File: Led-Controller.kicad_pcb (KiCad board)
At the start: 2 copper layers, 74.3 x 47.4 mm, 103 parts, among them J1 Program, J2 Barrel_Jack, J3 Screw_Terminal, J4 Screw_Terminal, J5 Ws2812 Conn, J6 Screw_Terminal, Q1 CSD18540Q5B, Q2 CSD18540Q5B, Q3 CSD18540Q5B, Q4 CSD18540Q5B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

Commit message: Review done
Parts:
- added C39: 33u, Capacitor_SMD:C_0603_1608Metric, F.Cu at (155.3, 102.3)
- added C40: 33u, Capacitor_SMD:C_0603_1608Metric, F.Cu at (157.0, 102.3)
- added H1: MountingHole, MountingHole:MountingHole_3.2mm_M3_DIN965_Pad, F.Cu at (171.8, 103.6)
- added H2: MountingHole, MountingHole:MountingHole_3.2mm_M3_DIN965_Pad, F.Cu at (107.3, 103.8)
- moved TP2 3.75 mm to (156.5, 105.6)
- moved J3 0.13 mm to (132.1, 64.1)
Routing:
- net +3.3V: track 55.4 -> 48.1 mm
- net GND: vias 117 -> 124
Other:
- board size 74.3 x 47.4 mm -> 72.1 x 47.4 mm

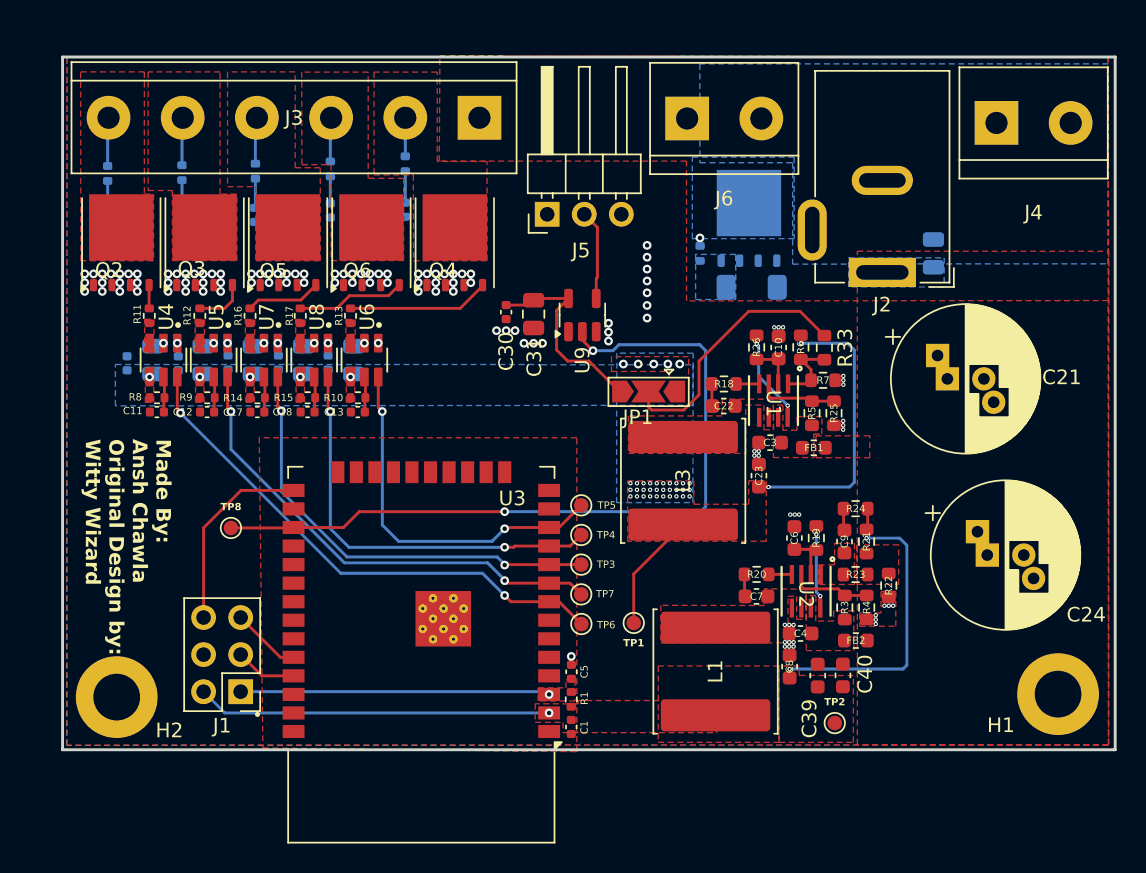
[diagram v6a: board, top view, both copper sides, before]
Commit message: WIP::Added: BOM for major components
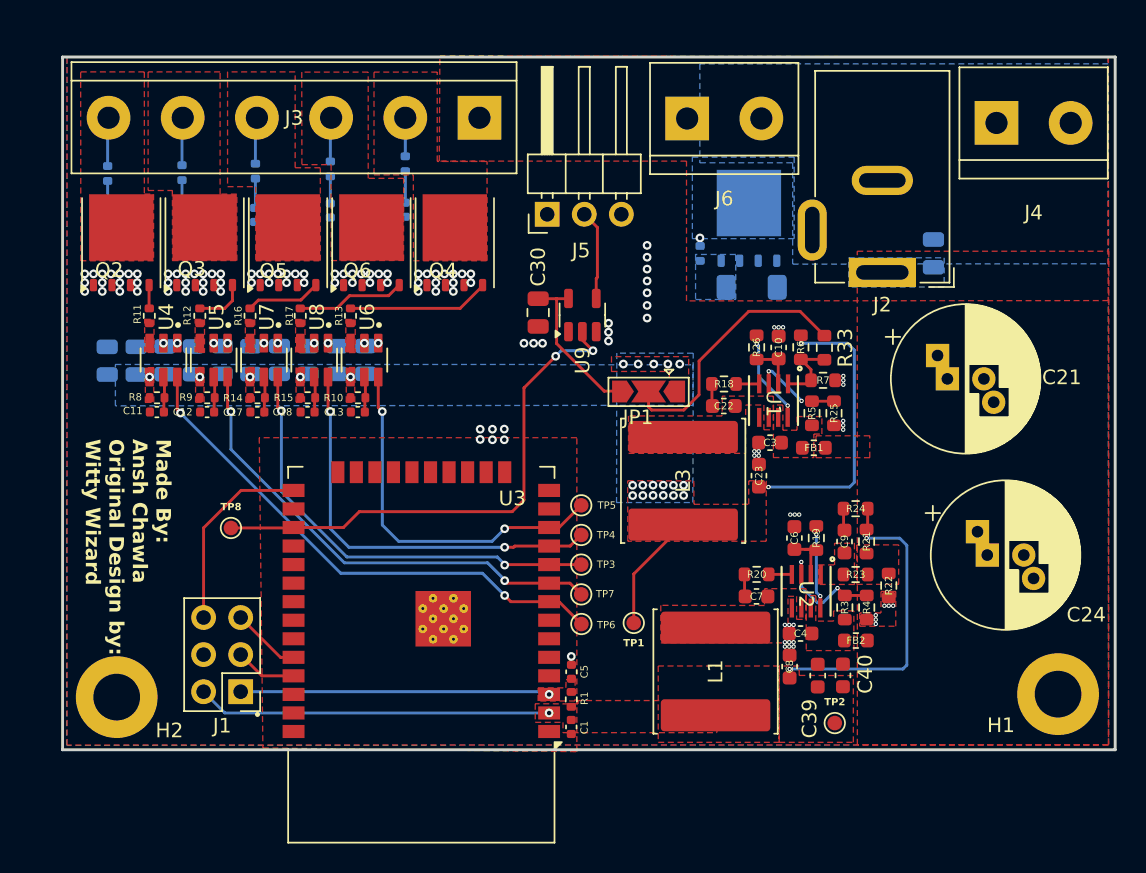
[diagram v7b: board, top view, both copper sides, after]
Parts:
- removed C31: 22uf, Capacitor_SMD:C_0805_2012Metric
- C25, C26, C27, C28, C29, C30: footprint Capacitor_SMD:C_0402_1005Metric -> Capacitor_SMD:C_0805_2012Metric
- moved C30 2.19 mm to (136.2, 77.5)
- moved C25 1.37 mm to (106.6, 80.7)
- moved C16 1.14 mm to (108.6, 80.7)
- moved C26 0.94 mm to (110.6, 80.7)
- moved C20 0.82 mm to (124.3, 80.7)
- moved C15 0.66 mm to (112.5, 80.7)
- moved C29 0.63 mm to (122.4, 80.7)
- moved C27 0.44 mm to (114.5, 80.7)
- moved C19 0.30 mm to (120.4, 80.7)
- moved C28 0.19 mm to (118.4, 80.7)
- moved C14 0.17 mm to (116.5, 80.7)
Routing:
- net /DOUT: track 53.5 -> 35.9 mm
- net +5V: track 13.8 -> 10.8 mm
- net Net-(U2-EN/SYNC): track 5.57 -> 8.04 mm, vias 0 -> 2
- net Net-(U1-EN/SYNC): track 5.69 -> 5.99 mm, vias 0 -> 2
- net GND: vias 124 -> 127
- net +9V: vias 42 -> 24

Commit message: review still pending , BOM finalized and changed to 0603
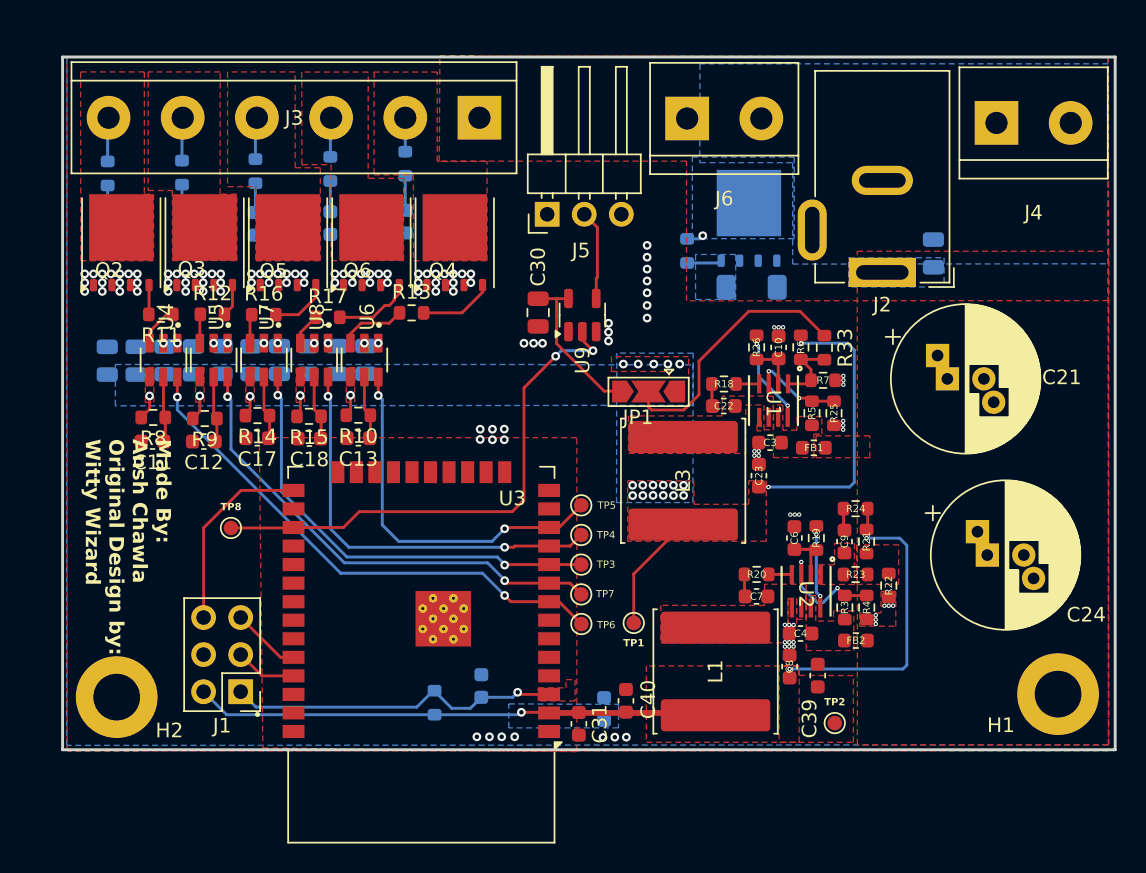
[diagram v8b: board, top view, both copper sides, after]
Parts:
- added C31: 0.1uf, Capacitor_SMD:C_0603_1608Metric, F.Cu at (138.9, 105.6)
- C1: footprint Capacitor_SMD:C_0402_1005Metric -> Capacitor_SMD:C_0603_1608Metric; moved to B.Cu
- C10, C22, C6, C7: value 100n -> 0.1uf
- C11, C12, C13, C17, C18, C32, C33, C34, C35, C36: value 100nf -> 0.1uf; footprint Capacitor_SMD:C_0402_1005Metric -> Capacitor_SMD:C_0603_1608Metric
- C23, C3, C39, C4, C40, C8: value 33u -> 22uf
- C25, C26, C27, C28, C29, C30: value 100nf -> 0.1uf
- C5: value 100nf -> 0.1uf; footprint Capacitor_SMD:C_0402_1005Metric -> Capacitor_SMD:C_0603_1608Metric; moved to B.Cu
- C9: value 33p -> 33pf
- D3: value ZMM7v5 -> ZMM7V5
- L1, L3: value 10u -> 10uH
- R1: footprint Resistor_SMD:R_0402_1005Metric -> Resistor_SMD:R_0603_1608Metric; moved to B.Cu
- R10, R11, R12, R13, R14, R15, R16, R17, R2, R8, R9: footprint Resistor_SMD:R_0402_1005Metric -> Resistor_SMD:R_0603_1608Metric
- R27, R28, R29, R30, R31: value 100 -> 100Ω; footprint Resistor_SMD:R_0402_1005Metric -> Resistor_SMD:R_0603_1608Metric
- moved C40 15.0 mm to (142.2, 104.0)
- moved R1 9.37 mm to (129.1, 104.2)
- moved C5 6.25 mm to (132.3, 103.0)
- moved R13 4.19 mm to (127.5, 77.5), turned to 0 degrees
- moved C1 2.56 mm to (140.7, 104.6), turned to 90 degrees
- moved C11 2.04 mm to (109.7, 86.3)
- moved C12 2.03 mm to (113.3, 86.3)
- moved R17 1.88 mm to (121.7, 77.8), turned to 0 degrees
- moved C18 1.82 mm to (120.5, 86.1)
- moved C13 1.79 mm to (123.8, 86.1)
- moved C17 1.79 mm to (116.9, 86.1)
- moved R9 1.44 mm to (113.3, 84.7)
- moved R8 1.37 mm to (109.8, 84.6)
- moved R15 1.28 mm to (120.5, 84.6)
- moved R14 1.22 mm to (116.9, 84.5)
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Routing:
- net +3.3V: track 48.1 -> 59.7 mm
- net +9V: track 27.7 -> 35.6 mm
- net Net-(Q4-G): track 9.74 -> 5.11 mm
- net Net-(U6-OUT): track 0.00 -> 4.59 mm
- net Net-(U4-OUT): track 0.03 -> 2.88 mm
- net Net-(D3-K): track 0.00 -> 2.39 mm
- net Net-(U8-OUT): track 0.00 -> 2.21 mm
- net Net-(U4-EN/~{FLT}): track 2.49 -> 4.56 mm
- net Net-(Q6-G): track 7.43 -> 5.40 mm
- net Net-(U5-EN/~{FLT}): track 2.53 -> 4.56 mm
- net Net-(U7-OUT): track 0.00 -> 1.99 mm
- net Net-(U5-OUT): track 0.00 -> 1.99 mm
- net Net-(U8-EN/~{FLT}): track 2.45 -> 4.42 mm
- net /EN: track 21.4 -> 23.4 mm
- net Net-(U6-EN/~{FLT}): track 2.45 -> 4.38 mm
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- added copper zone on B.Cu, net +3.3V
- removed copper zone on F.Cu, net Net-(U4-OUT)
- removed copper zone on F.Cu, net Net-(U5-OUT)
- removed copper zone on F.Cu, net Net-(U6-OUT)
- removed copper zone on F.Cu, net Net-(U7-OUT)
- removed copper zone on F.Cu, net Net-(U8-OUT)
